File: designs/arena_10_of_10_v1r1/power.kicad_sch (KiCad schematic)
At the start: 3 parts

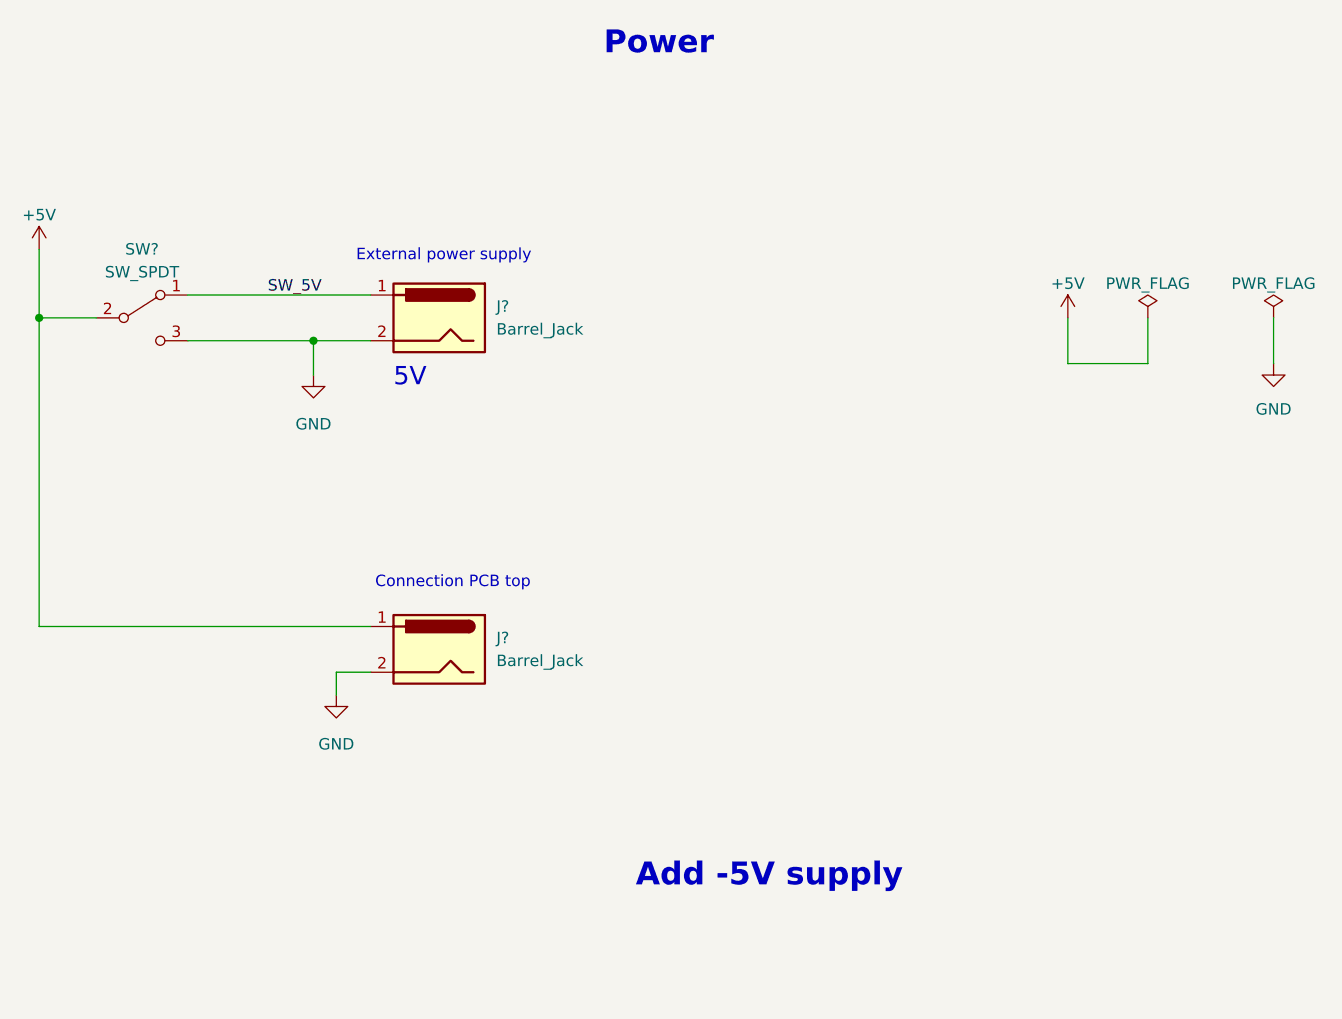
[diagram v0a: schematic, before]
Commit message: Re-worked MISO handling and analog input circuit.
Modified so that MISO isolation circuits are in fan out section and
are such that they will be placed close to the teensy.  Modified the
analog input circuit so that the teensy MCU analog inputs are used in
conjuction with a level shifting circuit.
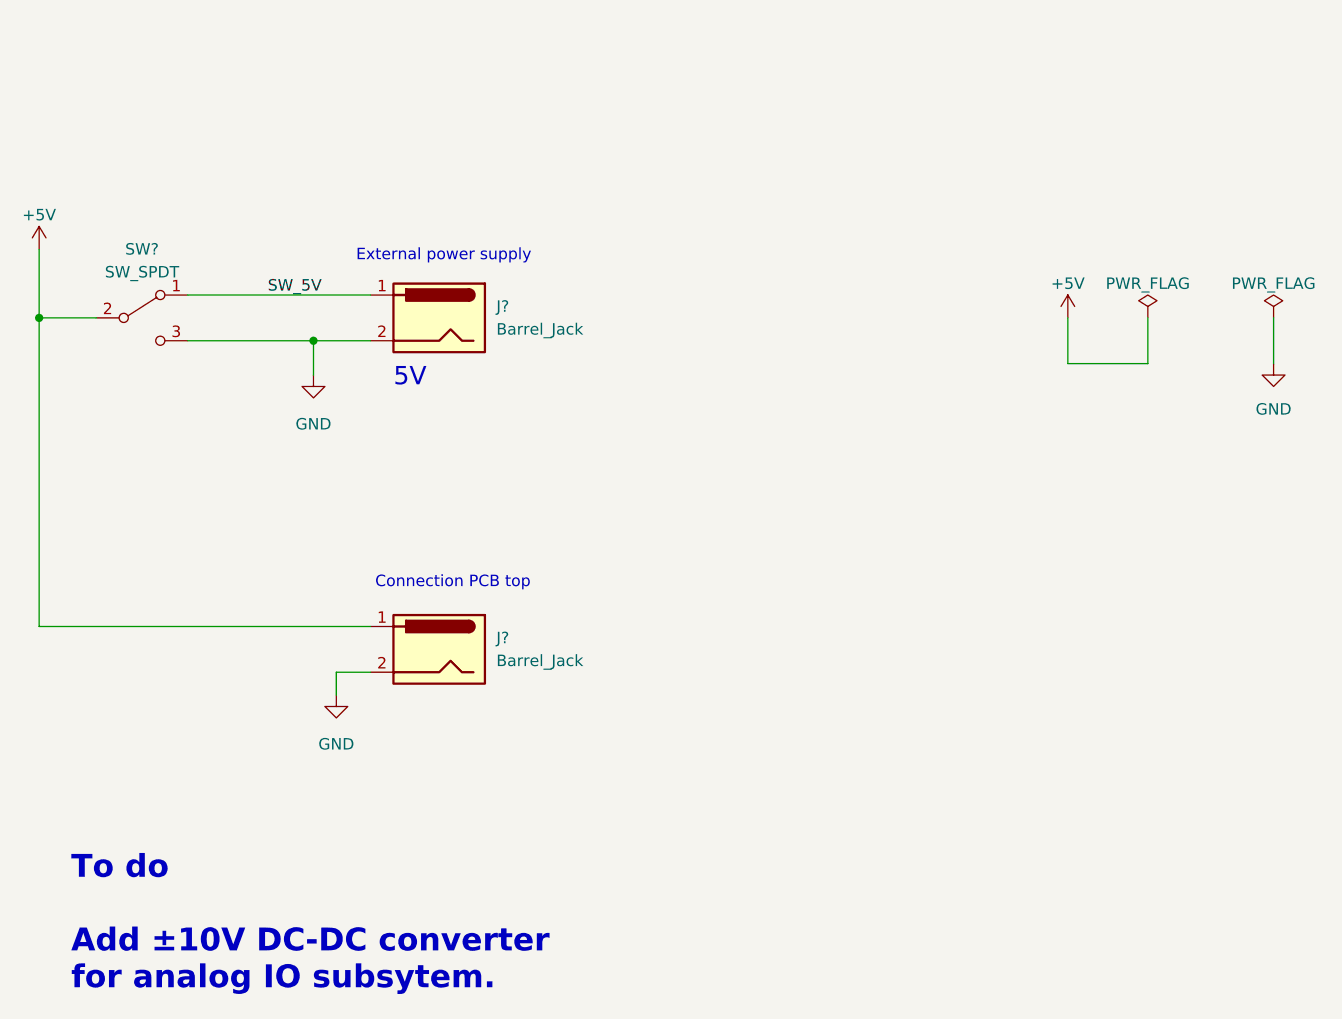
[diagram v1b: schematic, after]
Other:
- note added: "To do Add ±10V DC-DC converter for analog IO subsytem."
- note removed: "Add -5V supply"
- note removed: "Power"
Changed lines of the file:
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@@
-		)
-	)
-	(text "Power"
-		(exclude_from_sim no)
-		(at 142.748 25.654 0)
-		(effects
-			(font
-				(size 2.54 2.54)
-				(thickness 0.508)
-				(bold yes)
-			)
-			(justify left bottom)
 		)
 	)
@@
 		)
 	)
-	(text "Add -5V supply"
+	(text "To do\n\nAdd ±10V DC-DC converter\nfor analog IO subsytem. "
 		(exclude_from_sim no)
-		(at 146.304 118.11 0)
+		(at 83.566 129.54 0)
 		(effects
 			(font
